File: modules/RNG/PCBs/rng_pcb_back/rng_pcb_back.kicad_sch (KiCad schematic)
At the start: 30 parts, among them J10 Conn_01x08_Socket, J11 Eurorack_2x8_Power, J7 Conn_01x07_Socket, J8 Conn_02x03_Socket, J9 Conn_01x06_Socket, U1 TLC5940NT, U2 MCP4922, U3 MCP6004, U4 TL072, U5 LM4040BCZ-5

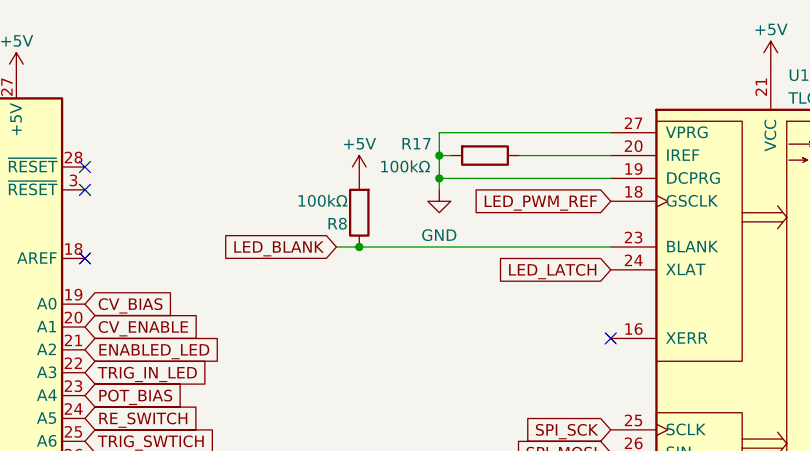
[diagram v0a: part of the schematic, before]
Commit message: added async analog reading to RNG
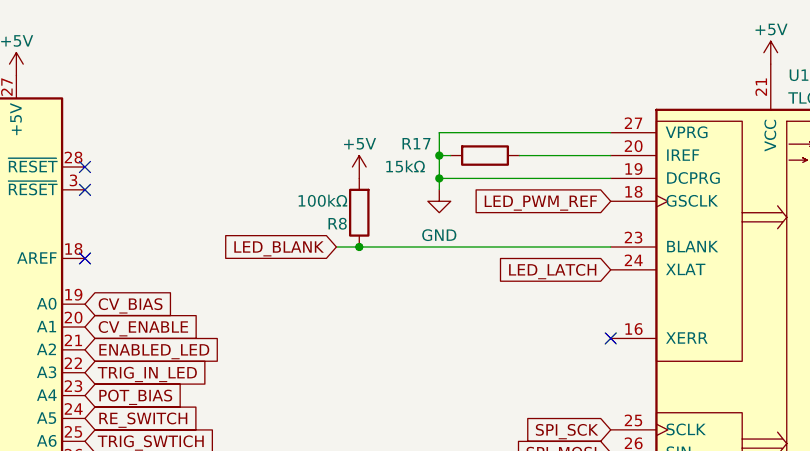
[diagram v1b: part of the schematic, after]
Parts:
- R17: value 100kΩ -> 15kΩ
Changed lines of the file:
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@@
       (effects (font (size 1.27 1.27)))
     )
-    (property "Value" "100kΩ" (at 104.14 34.29 90)
+    (property "Value" "15kΩ" (at 104.14 34.29 90)
       (effects (font (size 1.27 1.27)))
     )

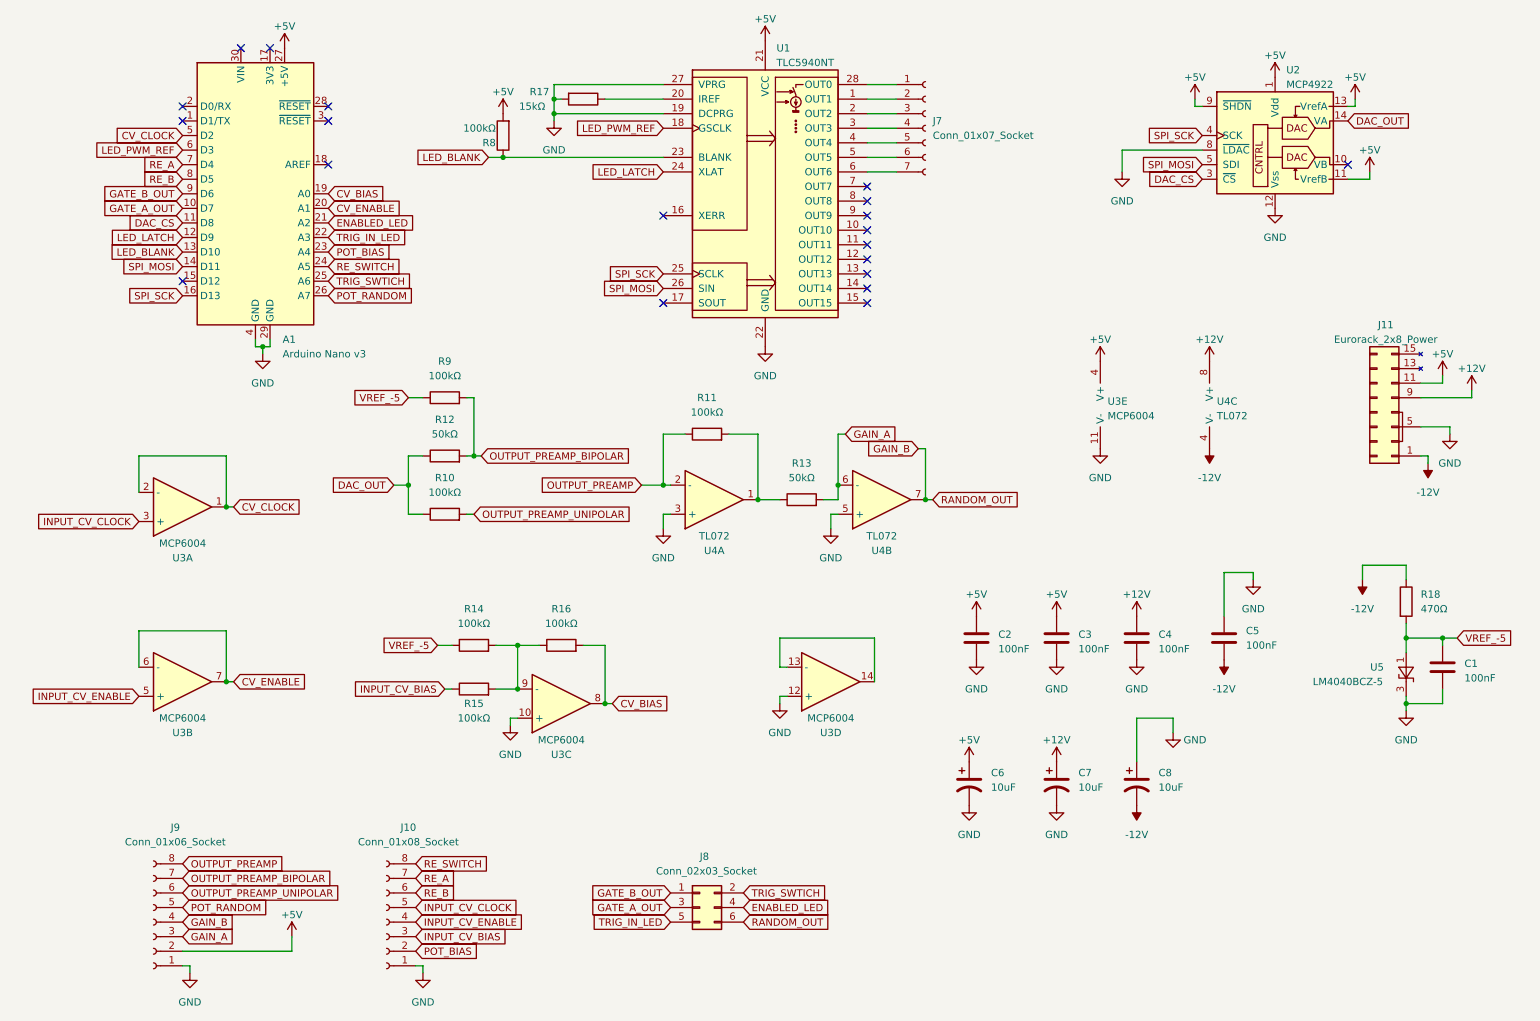
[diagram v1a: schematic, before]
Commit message: fix -5v ref in rng pcb
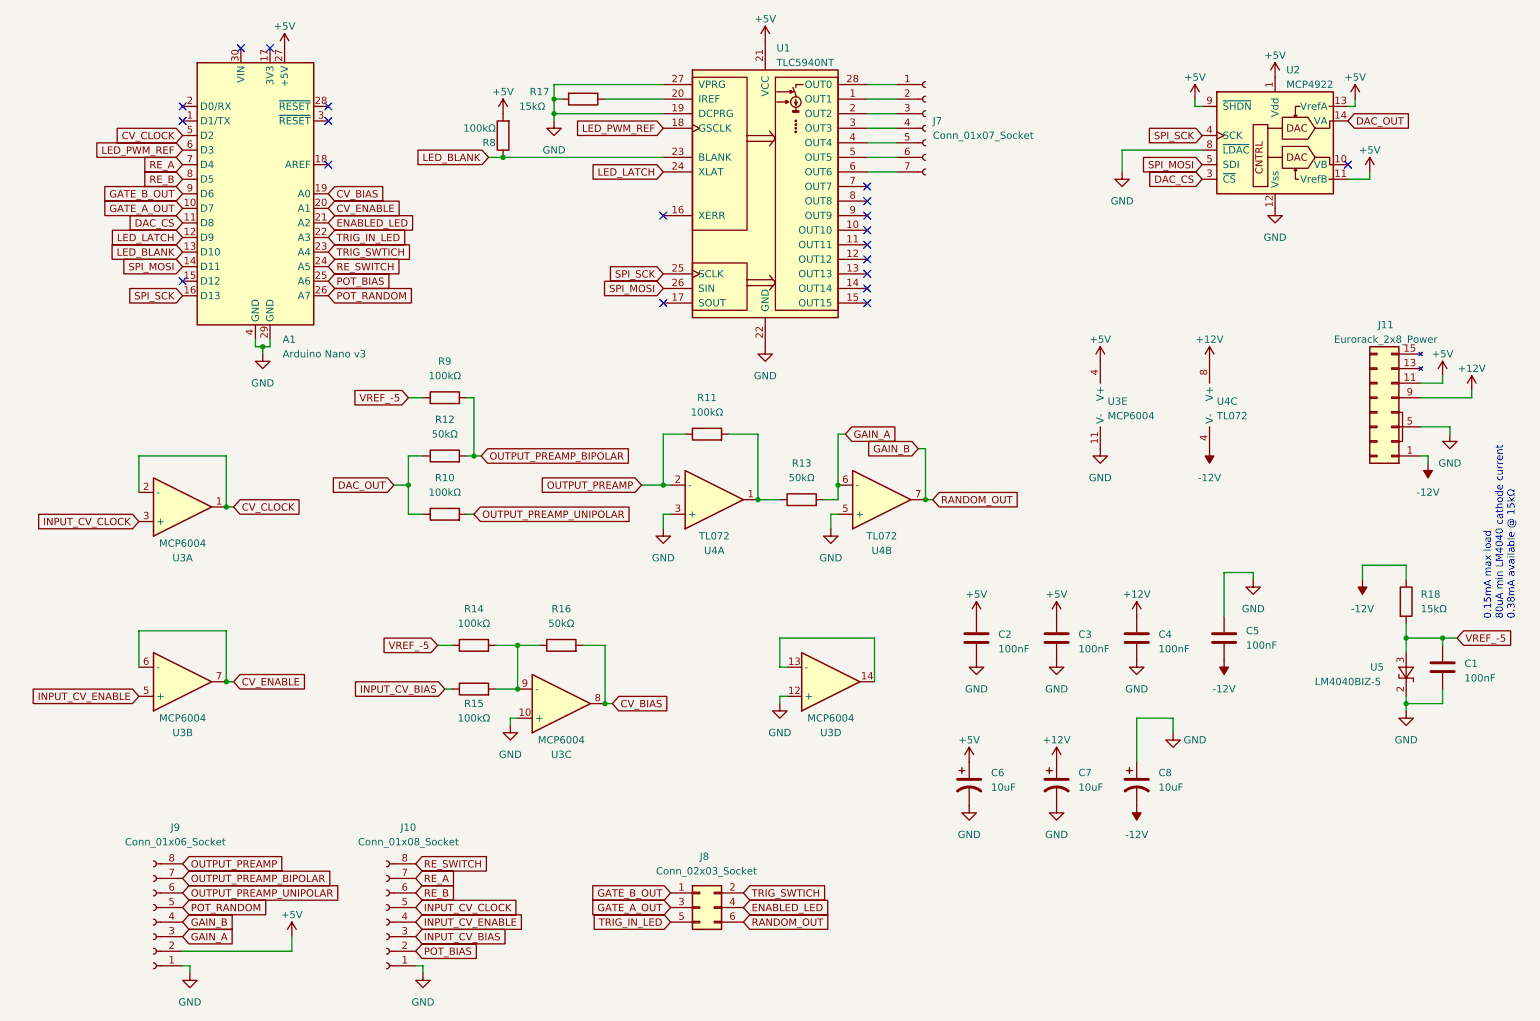
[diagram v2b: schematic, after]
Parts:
- R16: value 100kΩ -> 50kΩ
- R18: value 470Ω -> 15kΩ
- U5: value LM4040BCZ-5 -> LM4040BIZ-5; footprint Package_TO_SOT_THT:TO-92L_Inline_Wide -> Package_TO_SOT_THT:TO-92_Inline; symbol Reference_Voltage:LM4040DCK-5 -> Reference_Voltage:LM4040LP-5
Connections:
- net GND: now also U5.2 (K); no longer U5.3 (K)
- net POT_BIAS: now also A1.25 (A6); no longer A1.23 (A4)
- net TRIG_SWTICH: now also A1.23 (A4); no longer A1.25 (A6)
- net VREF_-5: now also U5.3 (A); no longer U5.1 (A)
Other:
- note added: "0.15mA max load 80uA min LM4040 cathode current 0.38mA available @ 15kΩ"
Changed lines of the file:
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@@
     (stroke (width 0) (type default))
   )
+  (text "0.15mA max load\n80uA min LM4040 cathode current\n0.38mA available @ 15kΩ"
+    (at 275.59 123.825 90)
+    (effects (font (size 1.27 1.27)) (justify left bottom))
+  )
   (global_label "GAIN_B" (shape input) (at 171.45 93.98 180) (fields_autoplaced)
     (effects (font (size 1.27 1.27)) (justify right))
@@
     )
   )
-  (global_label "TRIG_SWTICH" (shape input) (at 68.58 64.77 0) (fields_autoplaced)
-    (effects (font (size 1.27 1.27)) (justify left))
-    (property "Intersheetrefs" "${INTERSHEET_REFS}" (at 83.3996 64.77 0)
+  (global_label "TRIG_SWTICH" (shape input) (at 68.58 59.69 0) (fields_autoplaced)
+    (effects (font (size 1.27 1.27)) (justify left))
+    (property "Intersheetrefs" "${INTERSHEET_REFS}" (at 83.3996 59.69 0)
       (effects (font (size 1.27 1.27)) (justify left) hide)
     )
@@
     )
   )
-  (global_label "POT_BIAS" (shape input) (at 68.58 59.69 0) (fields_autoplaced)
-    (effects (font (size 1.27 1.27)) (justify left))
-    (property "Intersheetrefs" "${INTERSHEET_REFS}" (at 80.2738 59.69 0)
+  (global_label "POT_BIAS" (shape input) (at 68.58 64.77 0) (fields_autoplaced)
+    (effects (font (size 1.27 1.27)) (justify left))
+    (property "Intersheetrefs" "${INTERSHEET_REFS}" (at 80.2738 64.77 0)
       (effects (font (size 1.27 1.27)) (justify left) hide)
     )
@@
       (effects (font (size 1.27 1.27)))
     )
-    (property "Value" "100kΩ" (at 109.22 124.46 90)
+    (property "Value" "50kΩ" (at 109.22 124.46 90)
       (effects (font (size 1.27 1.27)))
     )
@@
     )
   )
-  (symbol (lib_id "Reference_Voltage:LM4040DCK-5") (at 256.54 133.35 270) (unit 1)
+  (symbol (lib_id "Reference_Voltage:LM4040LP-5") (at 256.54 133.35 270) (unit 1)
     (in_bom yes) (on_board yes) (dnp no)
     (property "Reference" "U5" (at 251.46 132.08 90)
       (effects (font (size 1.27 1.27)))
     )
-    (property "Value" "LM4040BCZ-5" (at 246.38 134.62 90)
-      (effects (font (size 1.27 1.27)))
-    )
-    (property "Footprint" "Package_TO_SOT_THT:TO-92L_Inline_Wide" (at 251.46 133.35 0)
+    (property "Value" "LM4040BIZ-5" (at 246.38 134.62 90)
+      (effects (font (size 1.27 1.27)))
+    )
+    (property "Footprint" "Package_TO_SOT_THT:TO-92_Inline" (at 251.46 133.35 0)
       (effects (font (size 1.27 1.27) italic) hide)
     )
@@
       (effects (font (size 1.27 1.27) italic) hide)
     )
-    (pin "1")
+    (pin "2")
     (pin "3")
     (instances
@@
       (effects (font (size 1.27 1.27)) (justify left))
     )
-    (property "Value" "470Ω" (at 259.08 121.92 0)
-      (effects (font (size 1.27 1.27)) (justify left))
-    )
+    (property "Value" "15kΩ" (at 259.08 121.92 0)
+      (effects (font (size 1.27 1.27)) (justify left))
+    )

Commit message: add missing output resistor
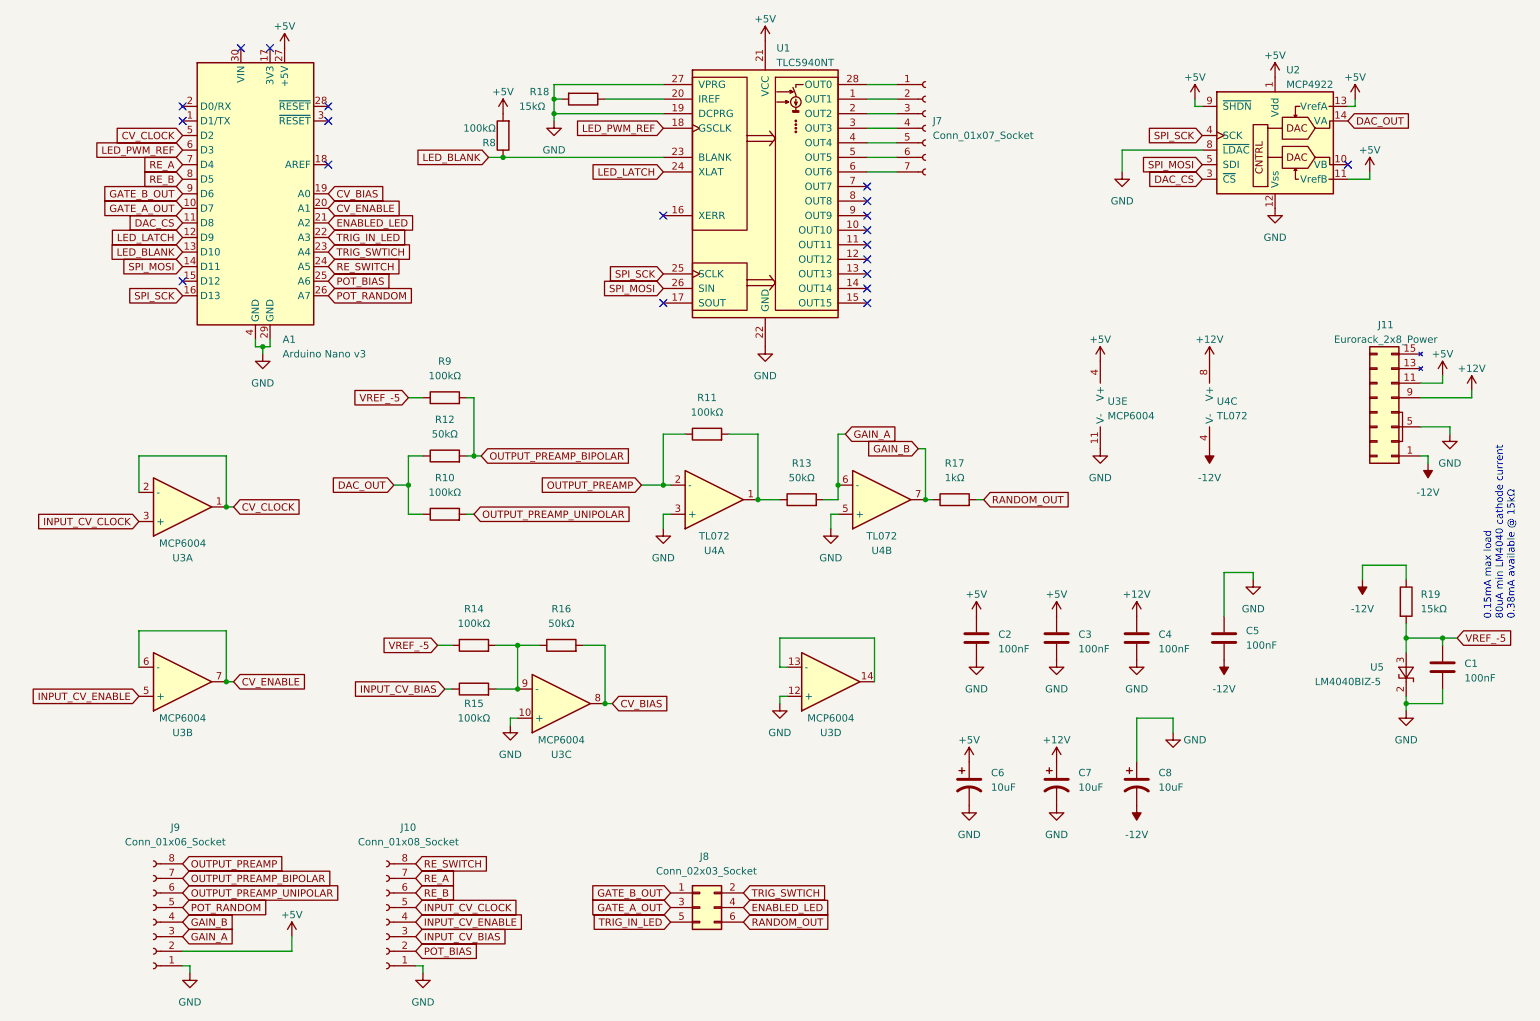
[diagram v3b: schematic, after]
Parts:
- added R17: 1kΩ, Resistor_THT:R_Axial_DIN0207_L6.3mm_D2.5mm_P7.62mm_Horizontal, symbol Device:R
- renumbered R17 to R18, R18 to R19
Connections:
- net GAIN_B: now also R17.1; no longer J8.6 (Pin_6)
- new net RANDOM_OUT: J8.6 (Pin_6), R17.2

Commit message: Add SMD option for LED driver on RNG
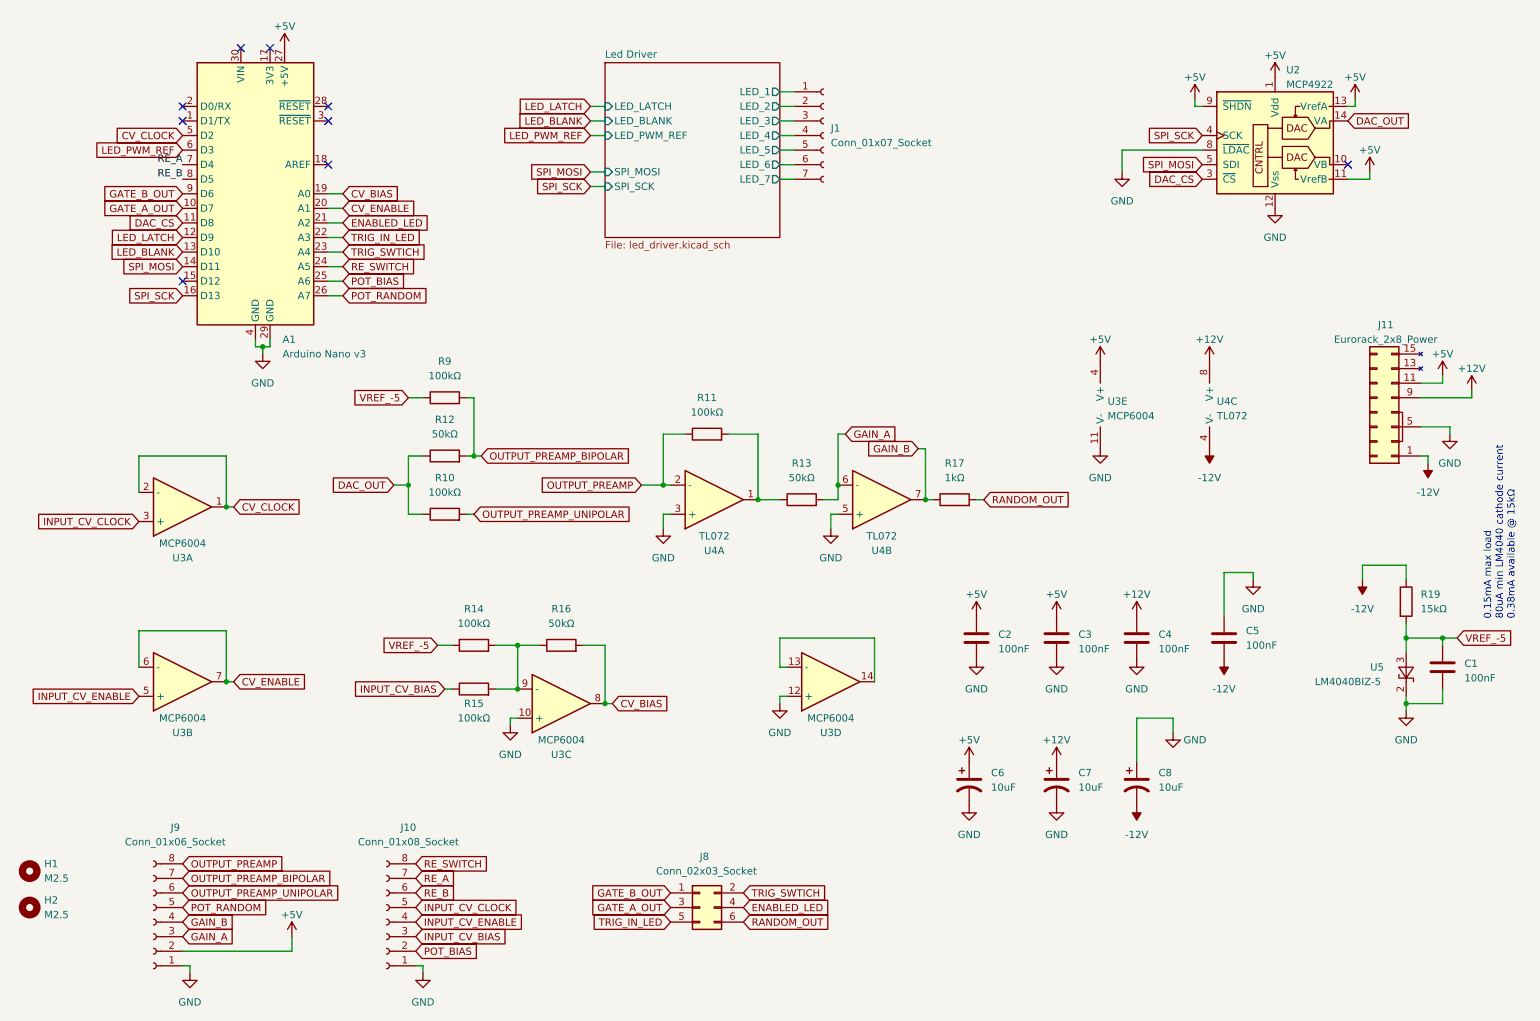
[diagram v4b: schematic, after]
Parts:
- removed J7: Conn_01x07_Socket, Connector_PinHeader_2.54mm:PinHeader_1x07_P2.54mm_Vertical, symbol Connector:Conn_01x07_Socket
- removed R18: 15kΩ, Resistor_THT:R_Axial_DIN0207_L6.3mm_D2.5mm_P7.62mm_Horizontal, symbol Device:R
- removed R8: 100kΩ, Resistor_THT:R_Axial_DIN0207_L6.3mm_D2.5mm_P7.62mm_Horizontal, symbol Device:R
- removed U1: TLC5940NT, Package_DIP:DIP-28_W7.62mm, symbol Driver_LED:TLC5940NT
- added H1, H2: M2.5, MountingHole:MountingHole_2.7mm_M2.5, symbol Mechanical:MountingHole
- added J1: Conn_01x07_Socket, Connector_PinHeader_2.54mm:PinHeader_1x07_P2.54mm_Vertical, symbol Connector:Conn_01x07_Socket
- U5: footprint Package_TO_SOT_THT:TO-92_Inline -> Package_TO_SOT_THT:TO-92_Inline_Wide
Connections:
- new net Led Driver/LED_1: J1.1 (Pin_1)
- new net Led Driver/LED_2: J1.2 (Pin_2)
- new net Led Driver/LED_3: J1.3 (Pin_3)
- new net Led Driver/LED_4: J1.4 (Pin_4)
- new net Led Driver/LED_5: J1.5 (Pin_5)
- new net Led Driver/LED_6: J1.6 (Pin_6)
- new net Led Driver/LED_7: J1.7 (Pin_7)
- no-connect marks 20 -> 9
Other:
- added sheet Led Driver (led_driver.kicad_sch)
- company: FreeModular -> Free Modular

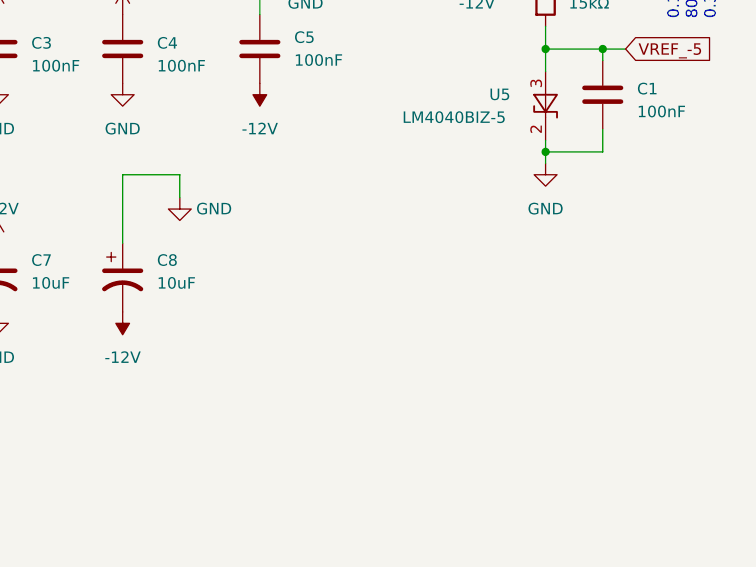
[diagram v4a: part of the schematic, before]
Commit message: Fix #55 and add decoupling capacitors
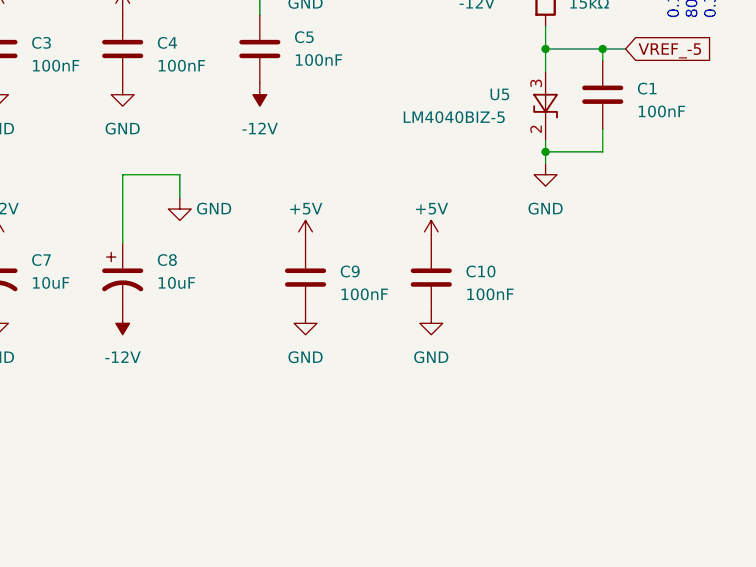
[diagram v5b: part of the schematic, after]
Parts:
- added C10, C9: 100nF, Capacitor_THT:C_Disc_D5.0mm_W2.5mm_P5.00mm, symbol Device:C
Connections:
- net +5V: now also C10.1, C9.1
- net GND: now also C10.2, C9.2
